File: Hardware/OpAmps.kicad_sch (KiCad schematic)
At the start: 56 parts, among them J7 Audio_Breakout, U10 TL074, U11 TL074, U12 TL074, U13 TL074, U14 TL074

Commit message: Added Gate ouputs to component board
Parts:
- added C56: 100nF, Capacitor_SMD:C_0603_1608Metric, symbol Device:C_Small
- added R86, R87, R88, R89: 10k, Resistor_SMD:R_0603_1608Metric, symbol Device:R_Small
- added R90, R91, R92, R93: 15k, Resistor_SMD:R_0603_1608Metric, symbol Device:R_Small
- added U15: TL074, Package_SO:TSSOP-14_4.4x5mm_P0.65mm, symbol Amplifier_Operational:TL074
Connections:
- net +12V: now also C56.1, U15.4 (V+)
- net -12V: now also U15.11 (V-)
- net GND: now also C56.2, R86.1, R87.1, R88.1, R89.1
- new net: R89.2, R93.2, U15.6 (-)
- new net: R87.2, R91.2, U15.13 (-)
- new net: R88.2, R92.2, U15.2 (-)
- new net: R86.2, R90.2, U15.9 (-)
- new net Gate1: U15.10 (+)
- new net Gate1_Out: R90.1, U15.8
- new net Gate2: U15.12 (+)
- new net Gate2_Out: R91.1, U15.14
- new net Gate3: U15.3 (+)
- new net Gate3_Out: R92.1, U15.1
- new net Gate4: U15.5 (+)
- new net Gate4_Out: R93.1, U15.7
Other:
- note added: "Gate Level Translation"
- moved on the sheet: C37, C38, C39, C40, C41, C42, C43, C44, C45, C46, R36, R37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

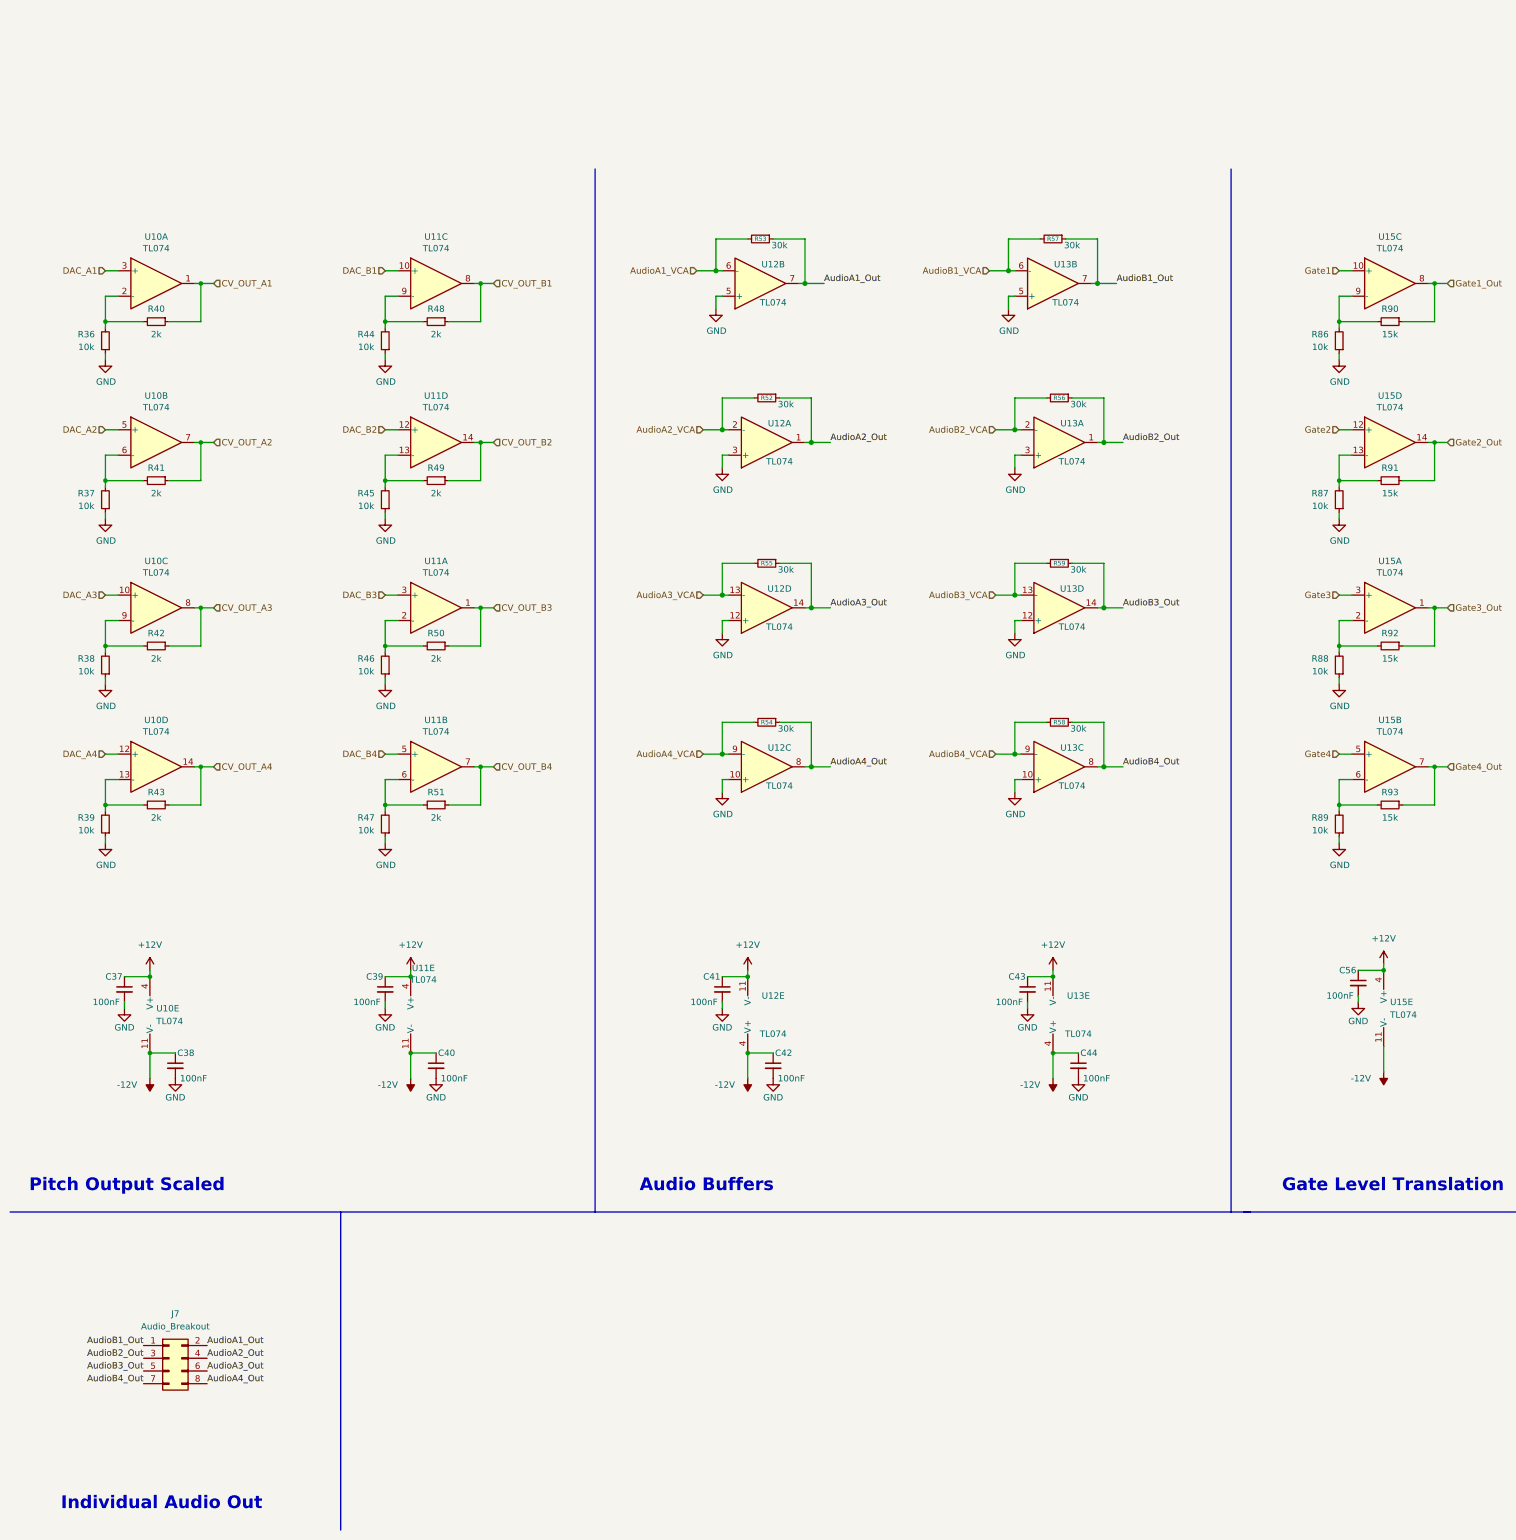
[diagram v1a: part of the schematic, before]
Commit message: Added breakout for gates on component board
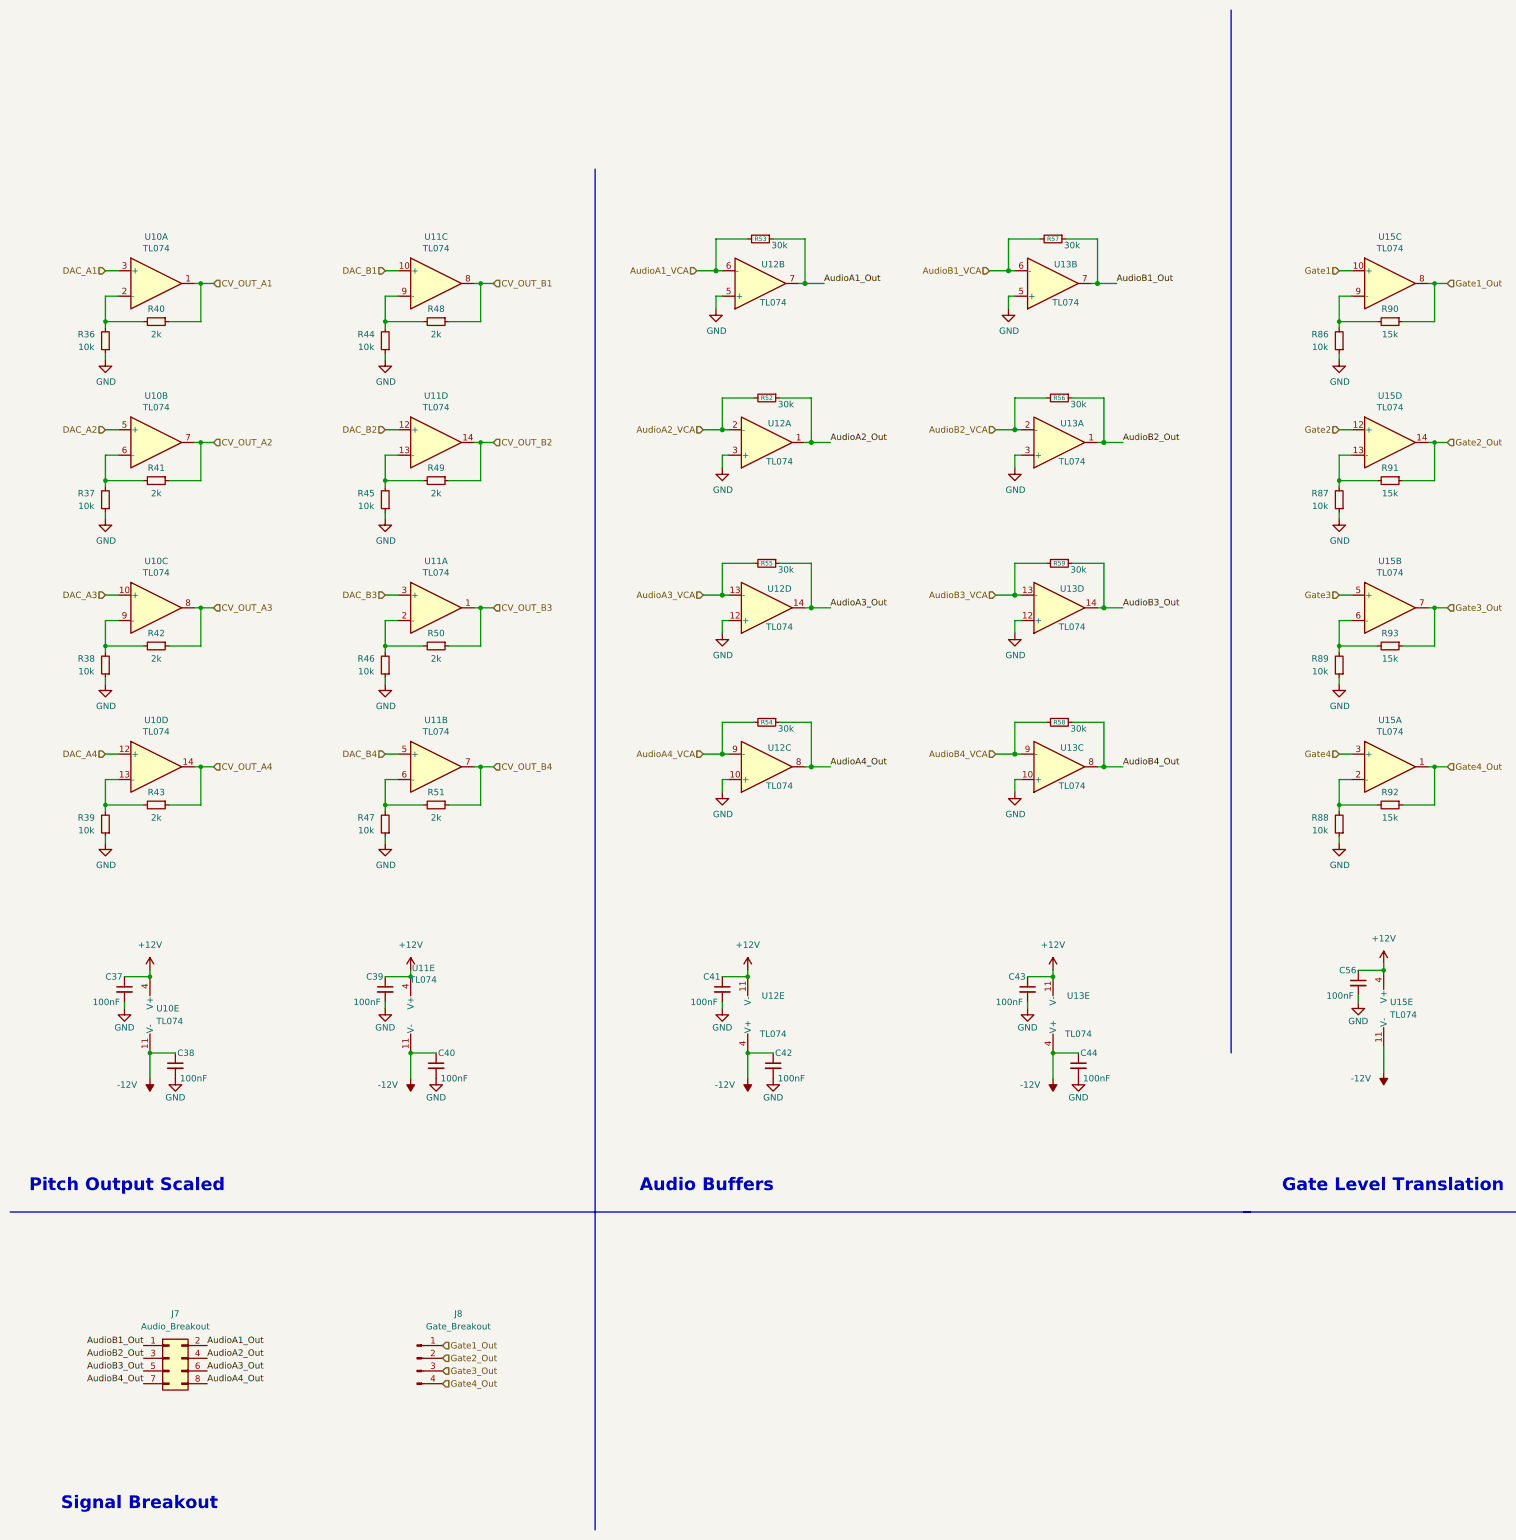
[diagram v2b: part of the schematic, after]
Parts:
- added J8: Gate_Breakout, Connector_PinHeader_2.54mm:PinHeader_1x04_P2.54mm_Vertical, symbol Connector:Conn_01x04_Male
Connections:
- net Gate1_Out: now also J8.1 (Pin_1)
- net Gate2_Out: now also J8.2 (Pin_2)
- net Gate3: now also U15.5 (+); no longer U15.3 (+)
- net Gate3_Out: now also R93.1, U15.7, J8.3 (Pin_3); no longer R92.1, U15.1
- net Gate4: now also U15.3 (+); no longer U15.5 (+)
- net Gate4_Out: now also R92.1, U15.1, J8.4 (Pin_4); no longer R93.1, U15.7
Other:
- note added: "Signal Breakout"
- note removed: "Individual Audio Out"
- moved on the sheet: R88, R89, R92, R93, U15A, U15B

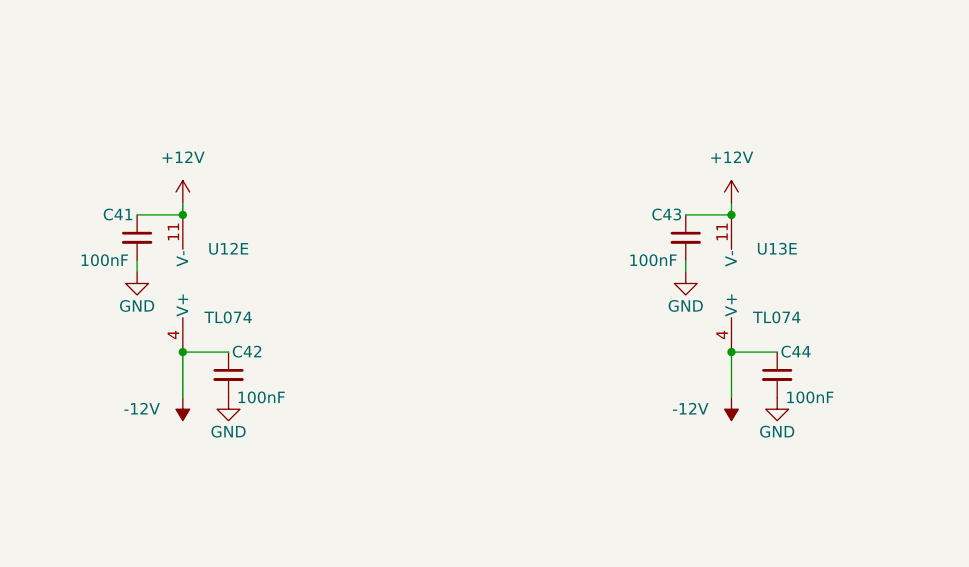
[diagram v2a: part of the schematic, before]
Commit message: Fixed OpAmp Power supply; component board annotations
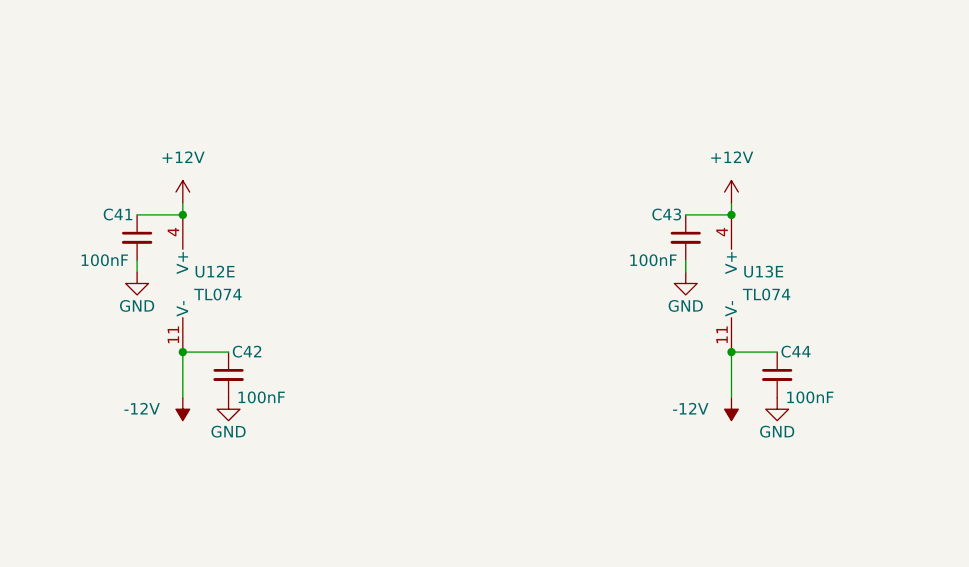
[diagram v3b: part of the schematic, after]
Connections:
- net +12V: now also U12.4 (V+), U13.4 (V+); no longer U12.11 (V-), U13.11 (V-)
- net -12V: now also U12.11 (V-), U13.11 (V-); no longer U12.4 (V+), U13.4 (V+)
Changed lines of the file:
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@@
   (junction (at 213.36 129.54) (diameter 1.016) (color 0 0 0 0)
   )
+  (junction (at 220.98 189.23) (diameter 0) (color 0 0 0 0)
+  )
   (junction (at 297.18 100.33) (diameter 0) (color 0 0 0 0)
   )
@@
   (junction (at 106.68 67.31) (diameter 0) (color 0 0 0 0)
   )
-  (junction (at 220.98 173.99) (diameter 0) (color 0 0 0 0)
+  (junction (at 160.02 173.99) (diameter 0) (color 0 0 0 0)
   )
   (junction (at 172.72 132.08) (diameter 1.016) (color 0 0 0 0)
@@
   (junction (at 297.18 67.31) (diameter 0) (color 0 0 0 0)
   )
+  (junction (at 220.98 173.99) (diameter 0) (color 0 0 0 0)
+  )
   (junction (at 154.94 97.79) (diameter 1.016) (color 0 0 0 0)
   )
@@
   (junction (at 358.14 64.77) (diameter 1.016) (color 0 0 0 0)
   )
+  (junction (at 160.02 189.23) (diameter 0) (color 0 0 0 0)
+  )
   (junction (at 40.64 173.99) (diameter 0) (color 0 0 0 0)
   )
@@
   (junction (at 106.68 132.08) (diameter 0) (color 0 0 0 0)
   )
-  (junction (at 160.02 173.99) (diameter 0) (color 0 0 0 0)
-  )
   (junction (at 154.94 64.77) (diameter 1.016) (color 0 0 0 0)
   )
@@
   (junction (at 106.68 35.56) (diameter 0) (color 0 0 0 0)
   )
-  (junction (at 160.02 189.23) (diameter 0) (color 0 0 0 0)
-  )
   (junction (at 231.14 132.08) (diameter 1.016) (color 0 0 0 0)
   )
@@
   (junction (at 172.72 100.33) (diameter 1.016) (color 0 0 0 0)
   )
-  (junction (at 220.98 189.23) (diameter 0) (color 0 0 0 0)
-  )
   (junction (at 287.02 172.72) (diameter 0) (color 0 0 0 0)
   )
@@
     (pin "4")
   )
-  (symbol (lib_id "Amplifier_Operational:TL074") (at 162.56 181.61 0) (mirror x) (unit 5)
-    (in_bom yes) (on_board yes)
-    (property "Reference" "U12" (id 0) (at 165.1 177.8 0))
-    (property "Value" "TL074" (id 1) (at 165.1 185.42 0))
-    (property "Footprint" "Package_SO:TSSOP-14_4.4x5mm_P0.65mm" (id 2) (at 161.29 184.15 0)
+  (symbol (lib_id "Amplifier_Operational:TL074") (at 157.48 181.61 0) (mirror y) (unit 5)
+    (in_bom yes) (on_board yes) (fields_autoplaced)
+    (property "Reference" "U12" (id 0) (at 161.29 180.3399 0)
+      (effects (font (size 1.27 1.27)) (justify right))
+    )
+    (property "Value" "TL074" (id 1) (at 161.29 182.8799 0)
+      (effects (font (size 1.27 1.27)) (justify right))
+    )
+    (property "Footprint" "Package_SO:TSSOP-14_4.4x5mm_P0.65mm" (id 2) (at 158.75 179.07 0)
       (effects (font (size 1.27 1.27)) hide)
     )
-    (property "Datasheet" "http://www.ti.com/lit/ds/symlink/tl071.pdf" (id 3) (at 163.83 186.69 0)
+    (property "Datasheet" "http://www.ti.com/lit/ds/symlink/tl071.pdf" (id 3) (at 156.21 176.53 0)
       (effects (font (size 1.27 1.27)) hide)
     )
@@
     (pin "2")
   )
-  (symbol (lib_id "Amplifier_Operational:TL074") (at 223.52 181.61 0) (mirror x) (unit 5)
-    (in_bom yes) (on_board yes)
-    (property "Reference" "U13" (id 0) (at 226.06 177.8 0))
-    (property "Value" "TL074" (id 1) (at 226.06 185.42 0))
-    (property "Footprint" "Package_SO:TSSOP-14_4.4x5mm_P0.65mm" (id 2) (at 222.25 184.15 0)
+  (symbol (lib_id "Amplifier_Operational:TL074") (at 218.44 181.61 0) (mirror y) (unit 5)
+    (in_bom yes) (on_board yes) (fields_autoplaced)
+    (property "Reference" "U13" (id 0) (at 222.25 180.3399 0)
+      (effects (font (size 1.27 1.27)) (justify right))
+    )
+    (property "Value" "TL074" (id 1) (at 222.25 182.8799 0)
+      (effects (font (size 1.27 1.27)) (justify right))
+    )
+    (property "Footprint" "Package_SO:TSSOP-14_4.4x5mm_P0.65mm" (id 2) (at 219.71 179.07 0)
       (effects (font (size 1.27 1.27)) hide)
     )
-    (property "Datasheet" "http://www.ti.com/lit/ds/symlink/tl071.pdf" (id 3) (at 224.79 186.69 0)
+    (property "Datasheet" "http://www.ti.com/lit/ds/symlink/tl071.pdf" (id 3) (at 217.17 176.53 0)
       (effects (font (size 1.27 1.27)) hide)
     )

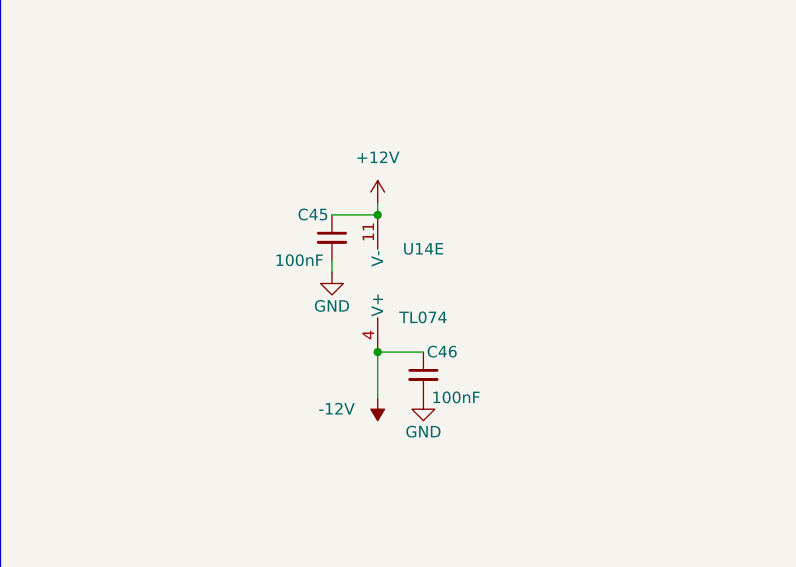
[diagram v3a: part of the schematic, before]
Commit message: Multiplexer tested working; PCB bug - U14 power rails inverted
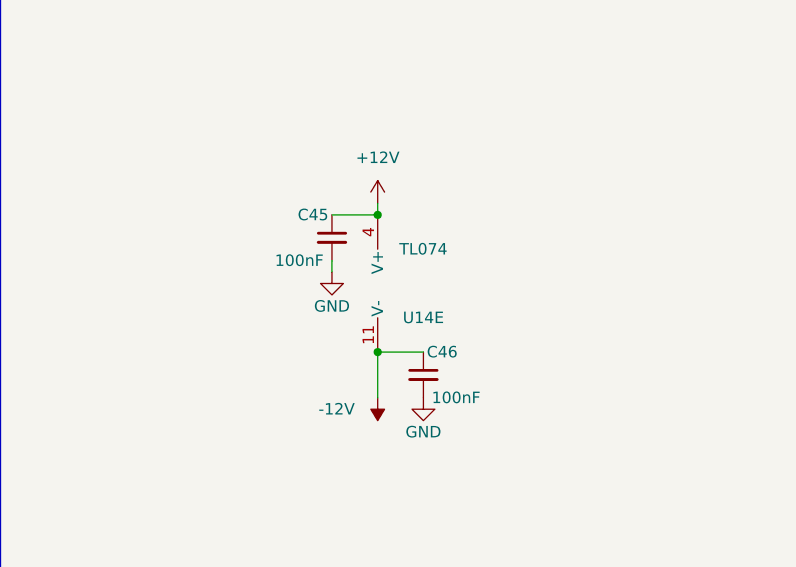
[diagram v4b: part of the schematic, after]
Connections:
- net +12V: now also U14.4 (V+); no longer U14.11 (V-)
- net -12V: now also U14.11 (V-); no longer U14.4 (V+)
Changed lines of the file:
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@@
     (pin "4")
   )
-  (symbol (lib_id "Amplifier_Operational:TL074") (at 365.76 181.61 0) (mirror x) (unit 5)
+  (symbol (lib_id "Amplifier_Operational:TL074") (at 365.76 181.61 0) (unit 5)
     (in_bom yes) (on_board yes)
-    (property "Reference" "U14" (id 0) (at 368.3 177.8 0))
-    (property "Value" "TL074" (id 1) (at 368.3 185.42 0))
-    (property "Footprint" "Package_SO:TSSOP-14_4.4x5mm_P0.65mm" (id 2) (at 364.49 184.15 0)
+    (property "Reference" "U14" (id 0) (at 368.3 185.42 0))
+    (property "Value" "TL074" (id 1) (at 368.3 177.8 0))
+    (property "Footprint" "Package_SO:TSSOP-14_4.4x5mm_P0.65mm" (id 2) (at 364.49 179.07 0)
       (effects (font (size 1.27 1.27)) hide)
     )
-    (property "Datasheet" "http://www.ti.com/lit/ds/symlink/tl071.pdf" (id 3) (at 367.03 186.69 0)
+    (property "Datasheet" "http://www.ti.com/lit/ds/symlink/tl071.pdf" (id 3) (at 367.03 176.53 0)
       (effects (font (size 1.27 1.27)) hide)
     )
